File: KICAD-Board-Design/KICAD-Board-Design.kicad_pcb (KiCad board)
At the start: 2 copper layers, 2 parts, among them J1 Conn_ARM_JTAG_SWD_10, U1 ESP32-WROOM-32D

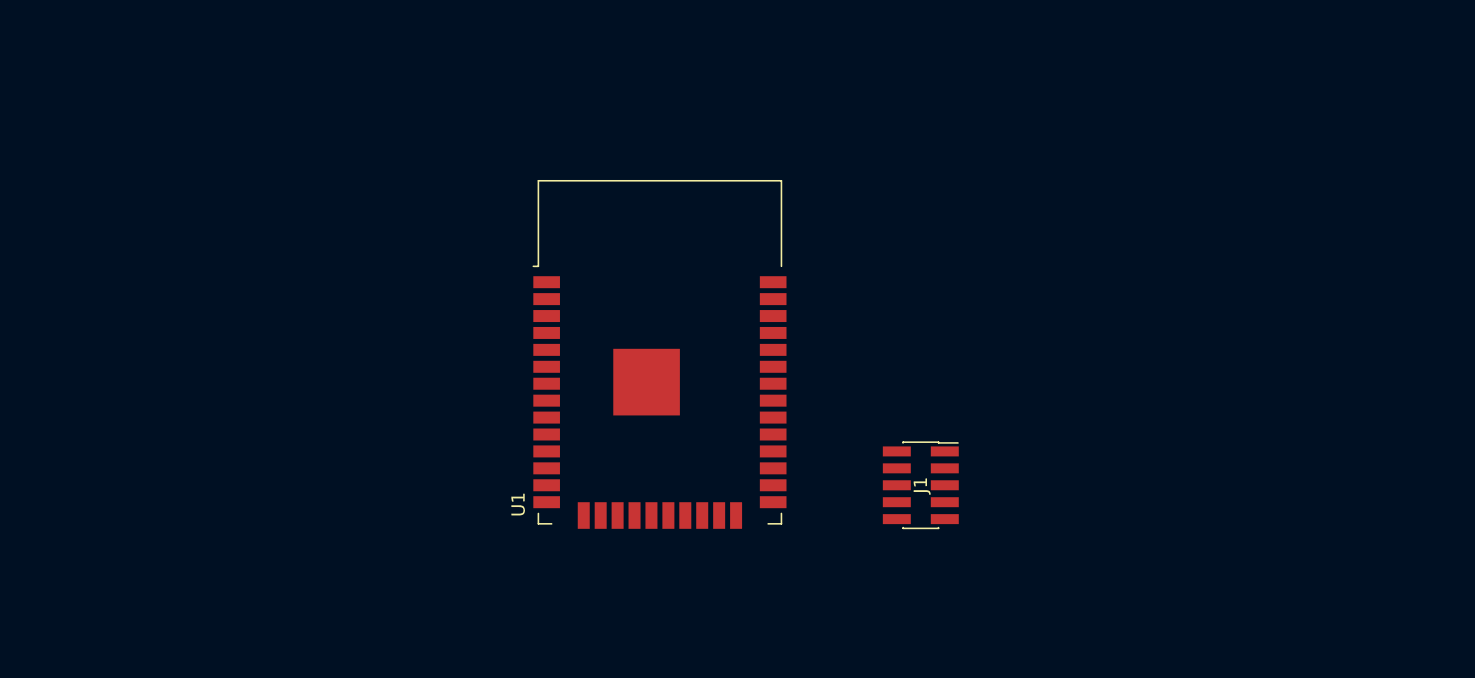
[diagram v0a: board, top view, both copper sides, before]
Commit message: Added Perf components
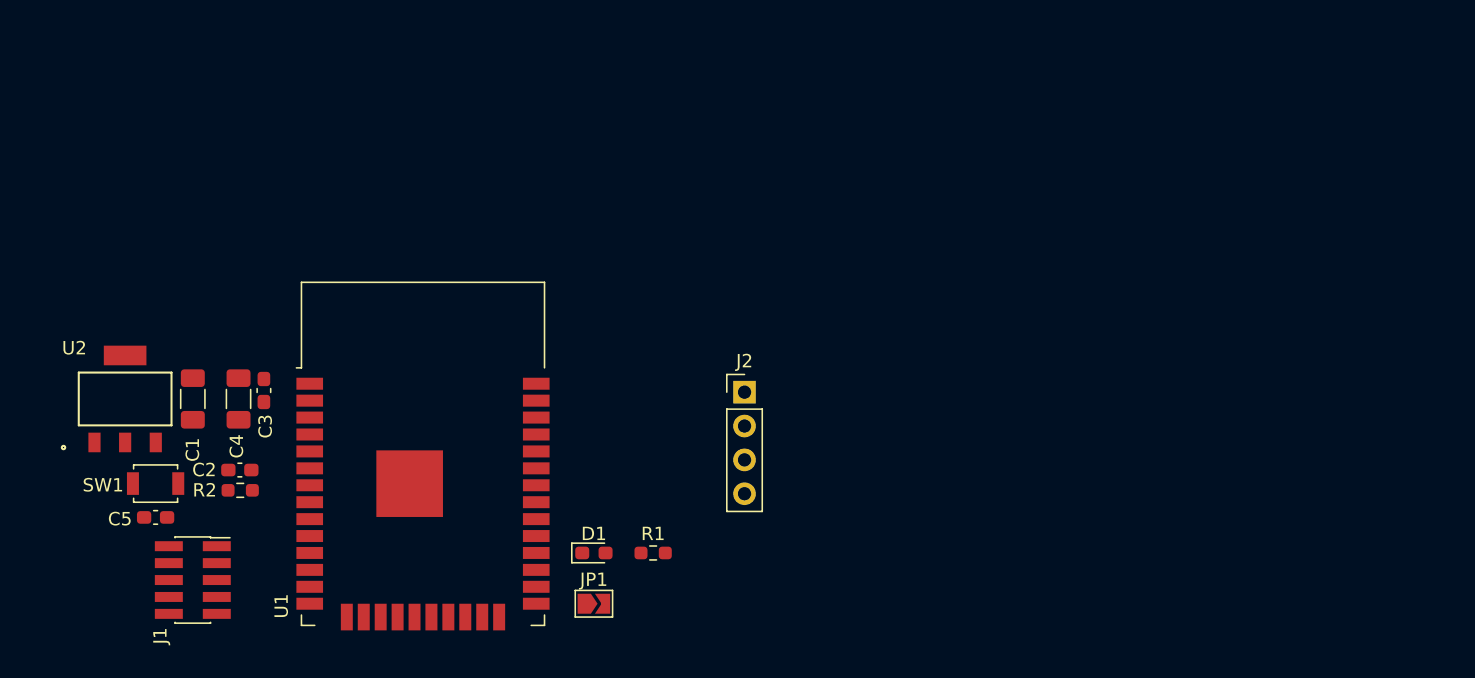
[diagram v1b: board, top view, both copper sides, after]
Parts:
- added C1: 10uF, Capacitor_SMD:C_1206_3216Metric_Pad1.33x1.80mm_HandSolder, F.Cu at (71.6, 118.0)
- added C2: 1uF, Capacitor_SMD:C_0603_1608Metric_Pad1.08x0.95mm_HandSolder, F.Cu at (75.2, 123.3)
- added C3: 0.1uF, Capacitor_SMD:C_0603_1608Metric_Pad1.08x0.95mm_HandSolder, F.Cu at (77.0, 117.3)
- added C4: 22uF, Capacitor_SMD:C_1206_3216Metric_Pad1.33x1.80mm_HandSolder, F.Cu at (75.1, 118.0)
- added C5: 0.1uF, Capacitor_SMD:C_0603_1608Metric_Pad1.08x0.95mm_HandSolder, F.Cu at (68.8, 126.9)
- added D1: LED, LED_SMD:LED_0603_1608Metric_Pad1.05x0.95mm_HandSolder, F.Cu at (101.7, 129.5)
- added J2: Conn_01x04, Connector_PinHeader_2.54mm:PinHeader_1x04_P2.54mm_Vertical, F.Cu at (113.0, 117.5)
- added JP1: Jumper_NO_Small, Jumper:SolderJumper-2_P1.3mm_Open_TrianglePad1.0x1.5mm, F.Cu at (101.7, 133.3)
- added R1: 68, Resistor_SMD:R_0603_1608Metric_Pad0.98x0.95mm_HandSolder, F.Cu at (106.2, 129.5)
- added R2: 10K, Resistor_SMD:R_0603_1608Metric_Pad0.98x0.95mm_HandSolder, F.Cu at (75.2, 124.8)
- added SW1: SW_Push, Button_Switch_SMD:SW_SPST_B3U-1000P, F.Cu at (68.8, 124.3)
- added U2: MIC5239-3.3YS-TR, Library-for-Components:MIC5239-3.3YS-TR, F.Cu at (66.5, 118.0)
- moved J1 55.1 mm to (71.6, 131.6)
- moved U1 19.3 mm to (88.9, 125.1)
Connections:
- J1 pad 10: /nReset -> (no net)
- J1 pad 7: Net-(J1-Pad7) -> (no net)
- U1 pad 1: Net-(U1-Pad1) -> GND
- U1 pad 10: Net-(U1-Pad10) -> (no net)
- U1 pad 11: Net-(U1-Pad11) -> (no net)
- U1 pad 12: Net-(U1-Pad12) -> (no net)
- U1 pad 13: Net-(U1-Pad13) -> /JTAG_TMS
- U1 pad 14: Net-(U1-Pad14) -> /JTAG_TDI
- U1 pad 15: Net-(U1-Pad1) -> GND
- U1 pad 16: Net-(U1-Pad16) -> /JTAG_TCK
- U1 pad 17: Net-(U1-Pad17) -> (no net)
- U1 pad 18: Net-(U1-Pad18) -> (no net)
- U1 pad 19: Net-(U1-Pad19) -> (no net)
- U1 pad 2: Net-(U1-Pad2) -> +3V3
- U1 pad 20: Net-(U1-Pad20) -> (no net)
- U1 pad 21: Net-(U1-Pad21) -> (no net)
- U1 pad 22: Net-(U1-Pad22) -> (no net)
- U1 pad 23: Net-(U1-Pad23) -> /JTAG_TDO
- U1 pad 24: Net-(U1-Pad24) -> (no net)
- U1 pad 26: Net-(U1-Pad26) -> (no net)
- U1 pad 27: Net-(U1-Pad27) -> (no net)
- U1 pad 28: Net-(U1-Pad28) -> (no net)
- U1 pad 29: Net-(U1-Pad29) -> (no net)
- U1 pad 30: Net-(U1-Pad30) -> (no net)
- U1 pad 31: Net-(U1-Pad31) -> (no net)
- U1 pad 32: Net-(U1-Pad32) -> (no net)
- U1 pad 33: Net-(U1-Pad33) -> (no net)
- U1 pad 34: Net-(U1-Pad34) -> /UART_RX
- U1 pad 35: Net-(U1-Pad35) -> /UART_TX
- U1 pad 36: Net-(U1-Pad36) -> (no net)
- U1 pad 37: Net-(U1-Pad37) -> (no net)
- U1 pad 38: Net-(U1-Pad1) -> GND
- U1 pad 39: Net-(U1-Pad1) -> GND
- U1 pad 4: Net-(U1-Pad4) -> (no net)
- U1 pad 5: Net-(U1-Pad5) -> (no net)
- U1 pad 6: Net-(U1-Pad6) -> (no net)
- U1 pad 7: Net-(U1-Pad7) -> (no net)
- U1 pad 8: Net-(U1-Pad8) -> (no net)
- U1 pad 9: Net-(U1-Pad9) -> (no net)

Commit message: Beginnging Layout
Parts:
- moved J2 11.7 mm to (102.9, 111.8)
- moved C1 6.68 mm to (70.6, 111.4)
- moved C2 6.68 mm to (74.1, 116.7)
- moved C3 6.68 mm to (75.9, 110.7)
- moved C4 6.68 mm to (74.0, 111.4)
- moved C5 6.68 mm to (67.8, 120.3)
- moved J1 6.68 mm to (70.6, 125.0)
- moved JP1 6.68 mm to (100.7, 126.7)
- moved SW1 6.68 mm to (67.8, 117.7)
- moved U1 6.68 mm to (87.9, 118.5)
- moved U2 6.68 mm to (65.5, 111.4)
- moved R2 6.68 mm to (74.2, 118.2)
- moved D1 6.68 mm to (100.7, 122.9)
- moved R1 6.68 mm to (105.2, 122.9)
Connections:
- C5 pad 1: Net-(C2-Pad1) -> GND
- C5 pad 2: GND -> Net-(C2-Pad1)
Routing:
- net /JTAG_TMS: track 0.00 -> 14.2 mm
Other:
- board outline added: 49.5 x 30.5 mm

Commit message: Layout Complete
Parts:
- added C6: 10uF, Capacitor_SMD:C_1206_3216Metric_Pad1.33x1.80mm_HandSolder, F.Cu at (119.0, 98.4)
- added C7: 22uF, Capacitor_SMD:C_1206_3216Metric_Pad1.33x1.80mm_HandSolder, F.Cu at (128.9, 102.7)
- added H1: MountingHole, MountingHole:MountingHole_2.7mm_M2.5, F.Cu at (118.6, 118.4)
- added H2: MountingHole, MountingHole:MountingHole_2.7mm_M2.5, F.Cu at (161.8, 118.4)
- added H3: MountingHole, MountingHole:MountingHole_2.7mm_M2.5, F.Cu at (161.8, 94.2)
- added H4: MountingHole, MountingHole:MountingHole_2.7mm_M2.5, F.Cu at (118.6, 94.2)
- added J3: Conn_01x02, TerminalBlock_TE-Connectivity:TerminalBlock_TE_282834-2_1x02_P2.54mm_Horizontal, F.Cu at (123.7, 95.5)
- added JP2: Jumper_NO_Small, Jumper:SolderJumper-2_P1.3mm_Open_TrianglePad1.0x1.5mm, F.Cu at (126.5, 111.0)
- added TP1: TestPoint, TestPoint:TestPoint_Keystone_5000-5004_Miniature, F.Cu at (159.5, 105.4)
- added TP2: TestPoint, TestPoint:TestPoint_Keystone_5000-5004_Miniature, F.Cu at (159.5, 99.3)
- added TP3: TestPoint, TestPoint:TestPoint_Keystone_5000-5004_Miniature, F.Cu at (132.3, 107.9)
- added TP4: TestPoint, TestPoint:TestPoint_Keystone_5000-5004_Miniature, F.Cu at (132.5, 111.8)
- J2: footprint Connector_PinHeader_2.54mm:PinHeader_1x04_P2.54mm_Vertical -> Connector_JST:JST_EH_B4B-EH-A_1x04_P2.50mm_Vertical
- U2: value MIC5239-3.3YS-TR -> AZ1117CH-3_3TRG1; footprint Library-for-Components:MIC5239-3.3YS-TR -> digikey-footprints:SOT-223
- moved J2 60.5 mm to (163.2, 106.9), turned to 90 degrees
- moved C3 58.3 mm to (133.2, 99.7)
- moved C4 58.3 mm to (131.3, 100.3)
- moved U1 57.5 mm to (144.3, 107.3)
- moved J1 56.7 mm to (126.8, 117.1), turned to 180 degrees
- moved C1 56.5 mm to (126.5, 102.7), turned to 270 degrees
- moved U2 55.7 mm to (120.7, 103.1), turned to 90 degrees
- moved D1 52.9 mm to (153.4, 118.7)
- moved R1 51.9 mm to (156.8, 118.7)
- moved C5 51.6 mm to (118.6, 111.0), turned to 0 degrees
- moved SW1 51.6 mm to (118.6, 108.5)
- moved JP1 49.6 mm to (149.9, 119.9), turned to 180 degrees
- moved C2 49.2 mm to (122.8, 109.5)
- moved R2 49.2 mm to (122.8, 111.0)
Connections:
- J1 pad 10: (no net) -> /nReset
- J1 pad 7: (no net) -> Net-(J1-Pad7)
- U1 pad 10: (no net) -> /ADC2_CH8
- U1 pad 11: (no net) -> /ADC2_CH9
- U1 pad 12: (no net) -> Net-(U1-Pad12)
- U1 pad 17: (no net) -> Net-(U1-Pad17)
- U1 pad 18: (no net) -> Net-(U1-Pad18)
- U1 pad 19: (no net) -> Net-(U1-Pad19)
- U1 pad 20: (no net) -> Net-(U1-Pad20)
- U1 pad 21: (no net) -> Net-(U1-Pad21)
- U1 pad 22: (no net) -> Net-(U1-Pad22)
- U1 pad 24: (no net) -> Net-(U1-Pad24)
- U1 pad 26: (no net) -> Net-(U1-Pad26)
- U1 pad 27: (no net) -> Net-(U1-Pad27)
- U1 pad 28: (no net) -> Net-(U1-Pad28)
- U1 pad 29: (no net) -> Net-(U1-Pad29)
- U1 pad 30: (no net) -> Net-(U1-Pad30)
- U1 pad 31: (no net) -> Net-(U1-Pad31)
- U1 pad 32: (no net) -> Net-(U1-Pad32)
- U1 pad 33: (no net) -> /I2C_SDA
- U1 pad 36: (no net) -> /I2C_SCL
- U1 pad 37: (no net) -> Net-(U1-Pad37)
- U1 pad 4: (no net) -> Net-(U1-Pad4)
- U1 pad 5: (no net) -> Net-(U1-Pad5)
- U1 pad 6: (no net) -> Net-(U1-Pad6)
- U1 pad 7: (no net) -> Net-(U1-Pad7)
- U1 pad 8: (no net) -> Net-(U1-Pad8)
- U1 pad 9: (no net) -> Net-(U1-Pad9)
- U2 pad 1: (no net) -> GND
- U2 pad 2: GND -> +3V3
- U2 pad 3: +3V3 -> +12V
- U2 pad 4: GND -> Net-(U2-Pad4)
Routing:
- net +3V3: track 0.00 -> 76.8 mm, vias 0 -> 3
- net Net-(C2-Pad1): track 0.00 -> 29.7 mm
- net /JTAG_TDO: track 0.00 -> 22.8 mm, vias 0 -> 2
- net /JTAG_TCK: track 0.00 -> 12.7 mm
- net /UART_RX: track 0.00 -> 11.1 mm
- net /UART_TX: track 0.00 -> 10.8 mm
- net +12V: track 0.00 -> 10.3 mm
- net /I2C_SCL: track 0.00 -> 7.69 mm
- net GND: track 0.00 -> 7.57 mm, vias 0 -> 4
- net /JTAG_TDI: track 0.00 -> 7.31 mm
- net /I2C_SDA: track 0.00 -> 6.74 mm
- net Net-(D1-Pad1): track 0.00 -> 6.08 mm
- net /nReset: track 0.00 -> 4.58 mm
- net /ADC2_CH8: track 0.00 -> 4.58 mm
- net /ADC2_CH9: track 0.00 -> 3.25 mm
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- added copper zone on B.Cu, net GND
- added copper zone on F.Cu, net GND
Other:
- board size 49.5 x 30.5 mm -> 49.5 x 31.8 mm
